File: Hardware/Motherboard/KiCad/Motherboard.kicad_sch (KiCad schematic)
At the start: 0 parts

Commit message: Added Motherboard schematic Rev. 1.0
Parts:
- added BZ1: Buzzer, Connector_PinHeader_2.54mm:PinHeader_1x02_P2.54mm_Vertical, symbol Device:Buzzer
- added C1: 10nF, Capacitor_SMD:C_1206_3216Metric_Pad1.33x1.80mm_HandSolder, symbol Device:C
- added C2: 100uF, Capacitor_SMD:CP_Elec_6.3x5.4, symbol Device:C_Polarized
- added D1: 1N4148WS, Diode_SMD:D_SOD-323_HandSoldering, symbol Device:D
- added H1, H2: M3, MountingHole:MountingHole_3.2mm_M3_Pad_Via, symbol Mechanical:MountingHole_Pad
- added J1: USB, Connector_PinHeader_2.54mm:PinHeader_1x04_P2.54mm_Vertical, symbol Connector_Generic:Conn_01x04
- added J2: FOLLOWER TUBE(S), Connector_PinHeader_2.54mm:PinHeader_1x03_P2.54mm_Vertical, symbol Connector_Generic:Conn_01x03
- added J3: MAIN TUBE(S), Connector_PinHeader_2.54mm:PinHeader_1x03_P2.54mm_Vertical, symbol Connector_Generic:Conn_01x03
- added Q1, Q2, Q3, Q4, Q5, Q6: MMBT3904, Package_TO_SOT_SMD:SOT-23, symbol Transistor_BJT:MMBT3904
- added Q7, Q8: MMBT3906, Package_TO_SOT_SMD:SOT-23, symbol Transistor_BJT:MMBT3906
- added R1: (Current Limit / Volume Adj.), Resistor_SMD:R_1206_3216Metric_Pad1.30x1.75mm_HandSolder, symbol Device:R
- added R10, R11, R12, R13, R14, R3, R4, R5, R6, R7, R8, R9: 10k, Resistor_SMD:R_1206_3216Metric_Pad1.30x1.75mm_HandSolder, symbol Device:R
- added R2: 1k, Resistor_SMD:R_1206_3216Metric_Pad1.30x1.75mm_HandSolder, symbol Device:R
- added U1: ~, Footprints:YD-ESP32-S3_(ESP32-S3-DevKitC-1_USB-C_Clone), symbol Symbols:YD-ESP32-S3_(ESP32-S3-DevKitC-1_USB-C_Clone)
- added U2: ~, Footprints:3.2in_SPI_TFT_Touch_Screen_&_SD_Card_Module, symbol Symbols:3.2in_SPI_TFT_Touch_Screen_&_SD_Card_Module
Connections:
- new net: Q8.1 (B), R8.1
- new net: Q3.3 (C), R7.2, R8.2
- new net: J2.2 (Pin_2), Q2.1 (B), R3.2
- new net: Q2.3 (C), R5.1, R6.1
- new net: Q5.3 (C), Q6.1 (B), R13.2
- new net: Q7.1 (B), R6.2
- new net: BZ1.1 (+), D1.1 (K), R1.2
- new net: BZ1.2 (-), D1.2 (A), Q1.3 (C)
- new net: Q4.1 (B), R12.1
- new net: Q4.3 (C), Q5.2 (E)
- new net: J3.2 (Pin_2), Q3.1 (B), R4.2
- new net: Q1.1 (B), R2.2
- new net: Q5.1 (B), R11.1
- new net: J1.3 (Pin_3), U1.25 (19)
- new net: J1.2 (Pin_2), U1.26 (20)
- new net +3V3: Q7.2 (E), Q8.2 (E), R13.1, R14.1, R5.2, R7.1, U1.1 (3V3), U1.2 (3V3)
- new net +5V: C1.1, C2.1, J1.1 (Pin_1), J2.1 (Pin_1), J3.1 (Pin_1), R1.1, U1.21 (5Vin), U2.1 (VCC)
- new net BUZZER: R2.1, U1.29 (48)
- new net COINCIDENCE_TRG: Q6.3 (C), R14.2, U1.37 (40)
- new net DISPLAY_CS: U1.11 (18), U2.3 (D_CS)
- new net DISPLAY_DC: U1.13 (3), U2.5 (D_DC)
- new net DISPLAY_LED: U1.15 (9), U2.8 (D_LED)
- new net DISPLAY_RST: U1.12 (8), U2.4 (D_RST)
- new net FOLLOWER_TRG: Q7.3 (C), R11.2, R9.2, U1.38 (41)
- new net GND: C1.2, C2.2, H1.1, H2.1, J1.4 (Pin_4), J2.3 (Pin_3), J3.3 (Pin_3), Q1.2 (E), Q2.2 (E), Q3.2 (E), Q4.2 (E), Q6.2 (E), R10.1, R3.1, R4.1, R9.1, U1.22 (GND), U1.23 (GND), U1.24 (GND), U1.44 (GND), U2.2 (GND)
- new net MAIN_TRG: Q8.3 (C), R10.2, R12.2, U1.39 (42)
- new net MISO: U1.19 (13), U2.13 (T_MISO), U2.17 (SD_MISO), U2.9 (D_MISO)
- new net MOSI: U1.17 (11), U2.12 (T_MOSI), U2.16 (SD_MOSI), U2.6 (D_MOSI)
- new net SCLK: U1.18 (12), U2.10 (T_SCLK), U2.18 (SD_SCLK), U2.7 (D_SCLK)
- new net SD_CD: U1.10 (17), U2.15 (SD_CS)
- new net TOUCH_CS: U1.16 (10), U2.11 (T_CS)
- new net TOUCH_IRQ: U1.20 (14), U2.14 (T_IRQ)
- no-connect marks 0 -> 21
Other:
- note added: "Buzzer Driver"
- note added: "Microcontroller"
- note added: "Mounting"
- note added: "Pulse Combiner & Coincidence Counter"
- note added: "Size: 3.2 inch Resolution: 240x320 px Display driver: ILI9341 Touch driver: XPT2046"
- note added: "Touchscreen & SD Card"
- note added: "YD-ESP32-S3 (ESP32-S3-DevKitC-1 USB-C Clone)"

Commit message: Motherboard PCB Rev. 1.0
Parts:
- J1: footprint Connector_PinHeader_2.54mm:PinHeader_1x04_P2.54mm_Vertical -> Footprints:USB_Pin_Header
- Q1, Q2, Q3, Q4, Q5, Q6, Q7, Q8: footprint Package_TO_SOT_SMD:SOT-23 -> Package_TO_SOT_SMD:SOT-23_Handsoldering
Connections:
- net BUZZER: now also U1.28 (47); no longer U1.29 (48)
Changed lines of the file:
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@@
 	(title_block
 		(title "Motherboard")
-		(date "2024-09-06")
+		(date "2024-09-07")
 		(rev "1.0")
 		(company "https://github.com/median-dispersion/GMT-Geiger-Counter")
@@
 	)
 	(no_connect
-		(at 236.22 77.47)
-	)
-	(no_connect
 		(at 236.22 62.23)
 	)
@@
 	)
 	(no_connect
+		(at 236.22 74.93)
+	)
+	(no_connect
 		(at 236.22 59.69)
 	)
@@
 	(wire
 		(pts
+			(xy 237.49 74.93) (xy 240.03 74.93)
+		)
+		(stroke
+			(width 0)
+			(type default)
+		)
+	)
+	(wire
+		(pts
 			(xy 240.03 90.17) (xy 256.54 90.17)
 		)
@@
 	(wire
 		(pts
+			(xy 236.22 77.47) (xy 237.49 77.47)
+		)
+		(stroke
+			(width 0)
+			(type default)
+		)
+	)
+	(wire
+		(pts
 			(xy 99.06 34.29) (xy 99.06 36.83)
 		)
@@
 	(wire
 		(pts
+			(xy 237.49 77.47) (xy 237.49 74.93)
+		)
+		(stroke
+			(width 0)
+			(type default)
+		)
+	)
+	(wire
+		(pts
 			(xy 214.63 146.05) (xy 214.63 140.97)
 		)
@@
 	(global_label "BUZZER"
 		(shape input)
-		(at 236.22 74.93 0)
+		(at 240.03 74.93 0)
 		(fields_autoplaced yes)
 		(effects
@@
 		)
 		(property "Intersheetrefs" "${INTERSHEET_REFS}"
-			(at 246.6437 74.93 0)
+			(at 250.4537 74.93 0)
 			(effects
 				(font
@@
 			)
 		)
-		(property "Footprint" "Package_TO_SOT_SMD:SOT-23"
+		(property "Footprint" "Package_TO_SOT_SMD:SOT-23_Handsoldering"
 			(at 77.47 53.975 0)
 			(effects
@@
 			)
 		)
-		(property "Footprint" "Package_TO_SOT_SMD:SOT-23"
+		(property "Footprint" "Package_TO_SOT_SMD:SOT-23_Handsoldering"
 			(at 92.71 43.815 0)
 			(effects
@@
 			)
 		)
-		(property "Footprint" "Package_TO_SOT_SMD:SOT-23"
+		(property "Footprint" "Package_TO_SOT_SMD:SOT-23_Handsoldering"
 			(at 116.84 56.515 0)
 			(effects
@@
 			)
 		)
-		(property "Footprint" "Package_TO_SOT_SMD:SOT-23"
+		(property "Footprint" "Package_TO_SOT_SMD:SOT-23_Handsoldering"
 			(at 134.62 92.075 0)
 			(effects
@@
 			)
 		)
-		(property "Footprint" "Package_TO_SOT_SMD:SOT-23"
+		(property "Footprint" "Package_TO_SOT_SMD:SOT-23_Handsoldering"
 			(at 57.15 154.305 0)
 			(effects
@@
 			)
 		)
-		(property "Footprint" "Package_TO_SOT_SMD:SOT-23"
+		(property "Footprint" "Package_TO_SOT_SMD:SOT-23_Handsoldering"
 			(at 134.62 81.915 0)
 			(effects
@@
 			)
 		)
-		(property "Footprint" "Package_TO_SOT_SMD:SOT-23"
+		(property "Footprint" "Package_TO_SOT_SMD:SOT-23_Handsoldering"
 			(at 101.6 66.675 0)
 			(effects
@@
 			)
 		)
-		(property "Footprint" "Package_TO_SOT_SMD:SOT-23"
+		(property "Footprint" "Package_TO_SOT_SMD:SOT-23_Handsoldering"
 			(at 149.86 74.295 0)
 			(effects
@@
 			)
 		)
-		(property "Footprint" "Connector_PinHeader_2.54mm:PinHeader_1x04_P2.54mm_Vertical"
+		(property "Footprint" "Footprints:USB_Pin_Header"
 			(at 246.38 82.55 0)
 			(effects

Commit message: Added BoM for motherboard
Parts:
- BZ1: DigiKey (none) -> https://www.digikey.com/en/products/detail/soberton-inc/WT-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; MPN (none) -> WT-1209T; Price (EUR) (none) -> 0,39€
- C1: DigiKey (none) -> https://www.digikey.com/en/products/detail/w%C3%BCrth-elekt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; MPN (none) -> 885012208112; Price (EUR) (none) -> 0,1€
- C2: DigiKey (none) -> https://www.digikey.com/en/products/detail/w%C3%BCrth-elekt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; MPN (none) -> 865080243007; Price (EUR) (none) -> 0,25€
- D1: DigiKey (none) -> https://www.digikey.com/en/products/detail/smc-diode-soluti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; MPN (none) -> 1N4148WS; Price (EUR) (none) -> 0,09€
- J1: DigiKey (none) -> https://www.digikey.com/en/products/detail/adam-tech/PH1RB-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; MPN (none) -> PH1RB-04-UA; Price (EUR) (none) -> 0,14€
- J2, J3: DigiKey (none) -> https://www.digikey.com/en/products/detail/adam-tech/PH1RB-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; MPN (none) -> PH1RB-03-UA; Price (EUR) (none) -> 0,11€
- Q1, Q2, Q3, Q4, Q5, Q6: DigiKey (none) -> https://www.digikey.com/en/products/detail/good-ark-semicon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; MPN (none) -> MMBT3904; Price (EUR) (none) -> 0,09€
- Q7, Q8: DigiKey (none) -> https://www.digikey.com/en/products/detail/good-ark-semicon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; MPN (none) -> MMBT3906; Price (EUR) (none) -> 0,09€
- R1: DigiKey (none) -> https://www.digikey.com/en/products/detail/yageo/RC1206JR-0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; MPN (none) -> RC1206JR-070RL; Price (EUR) (none) -> 0,09€
- R10, R11, R12, R13, R14, R3, R4, R5, R6, R7, R8, R9: DigiKey (none) -> https://www.digikey.com/en/products/detail/yageo/RC1206FR-1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; MPN (none) -> RC1206FR-1310KL; Price (EUR) (none) -> 0,09€
- R2: DigiKey (none) -> https://www.digikey.com/en/products/detail/yageo/RC1206FR-0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; MPN (none) -> RC1206FR-071KL; Price (EUR) (none) -> 0,09€
- U1: value ~ -> YD-ESP32-S3 N16R8 (ESP32-S3-DevKitC-1 USB-C Clone); MPN (none) -> YD-ESP32-S3 N16R8; Price (EUR) (none) -> 8€
- U2: value ~ -> MSP3218; MPN (none) -> MSP3218; Price (EUR) (none) -> 12€
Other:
- note removed: "YD-ESP32-S3 (ESP32-S3-DevKitC-1 USB-C Clone)"

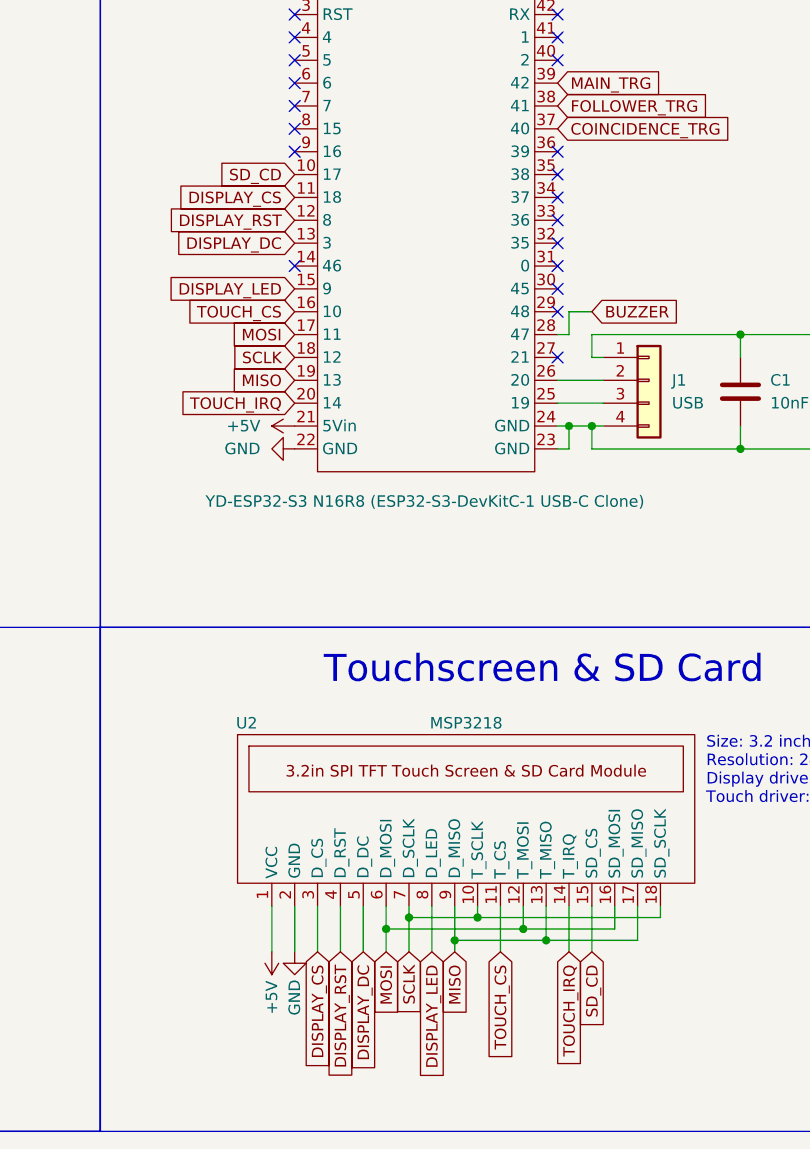
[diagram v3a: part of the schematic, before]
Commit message: Changed component value, fixed typos & fixed small mistakes
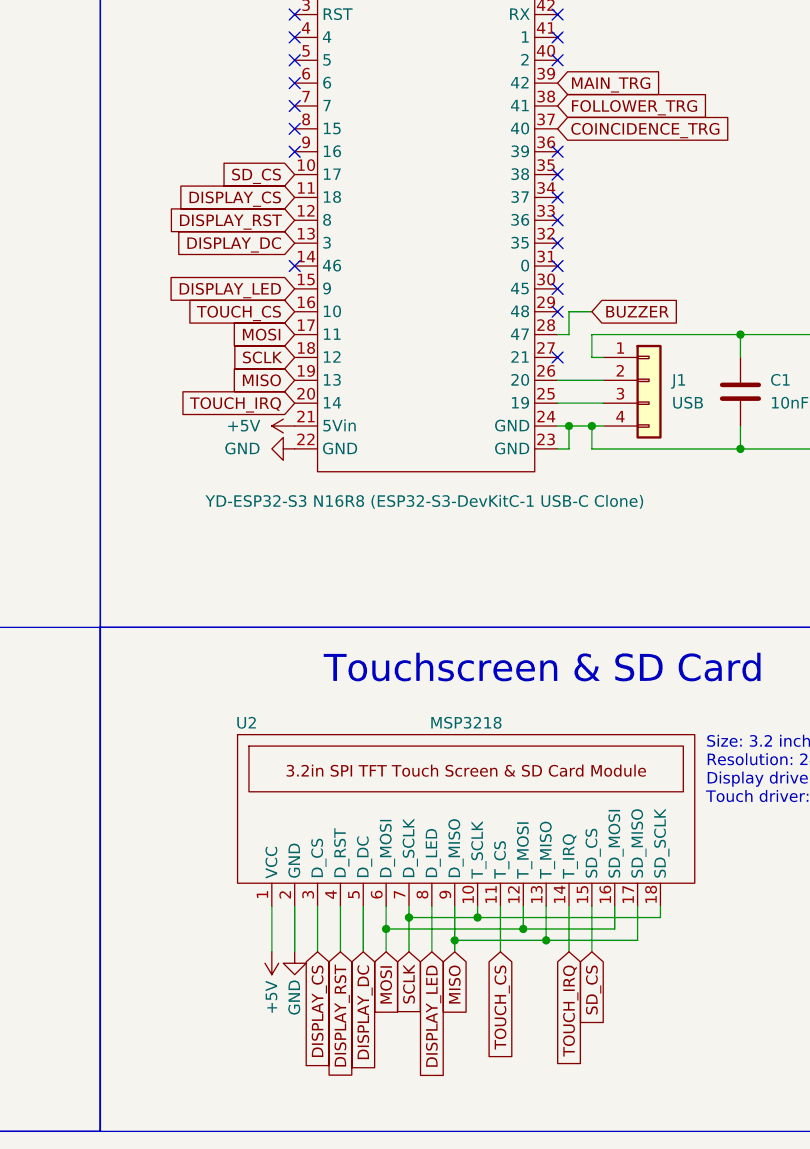
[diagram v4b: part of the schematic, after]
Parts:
- C2: DigiKey https://www.digikey.com/en/products/detail/w%C3%BCrth-elekt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 -> https://www.digikey.com/en/products/detail/würth-elektronik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; MPN 865080243007 -> 875105344010; Price (EUR) 0,25€ -> 0,62€
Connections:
- net SD_CD renamed SD_CS
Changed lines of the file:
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@@
 	(title_block
 		(title "Motherboard")
-		(date "2024-09-10")
+		(date "2024-11-14")
 		(rev "1.0")
 		(company "https://github.com/median-dispersion/GMT-Geiger-Counter")
@@
 		)
 	)
-	(global_label "SD_CD"
+	(global_label "SD_CS"
 		(shape input)
 		(at 207.01 59.69 180)
@@
 		)
 		(property "Intersheetrefs" "${INTERSHEET_REFS}"
-			(at 198.0377 59.69 0)
+			(at 198.0982 59.69 0)
 			(effects
 				(font
@@
 		)
 	)
-	(global_label "SD_CD"
+	(global_label "SD_CS"
 		(shape input)
 		(at 240.03 146.05 270)
@@
 		)
 		(property "Intersheetrefs" "${INTERSHEET_REFS}"
-			(at 240.03 155.0223 90)
+			(at 240.03 154.9618 90)
 			(effects
 				(font
@@
 			)
 		)
-		(property "Datasheet" "https://www.we-online.com/components/products/datasheet/865080243007.pdf"
+		(property "Datasheet" "https://www.we-online.com/components/products/datasheet/875105344010.pdf"
 			(at 267.97 83.82 0)
 			(effects
@@
 			)
 		)
-		(property "DigiKey" "https://www.digikey.com/en/products/detail/w%C3%BCrth-elektronik/865080243007/5728085 "
+		(property "DigiKey" "https://www.digikey.com/en/products/detail/würth-elektronik/875105344010/5147589"
 			(at 267.97 83.82 0)
 			(effects
@@
 			)
 		)
-		(property "MPN" "865080243007 "
+		(property "MPN" "875105344010"
 			(at 267.97 83.82 0)
 			(effects
@@
 			)
 		)
-		(property "Price (EUR)" "0,25€ "
+		(property "Price (EUR)" "0,62€"
 			(at 267.97 83.82 0)
 			(effects

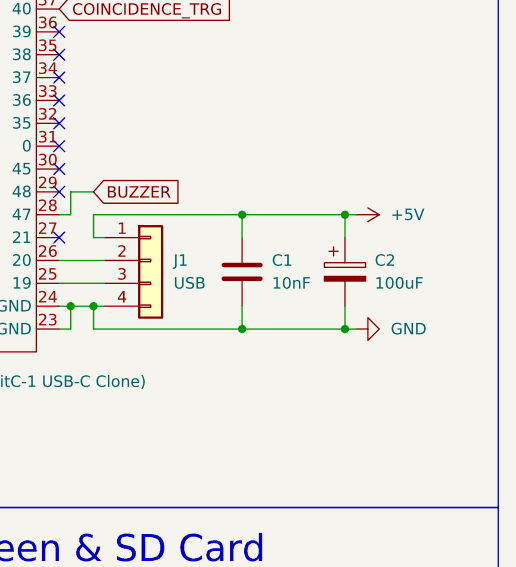
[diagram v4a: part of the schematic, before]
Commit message: Updated the decoupling capacitor to make it more USB 'compliant'
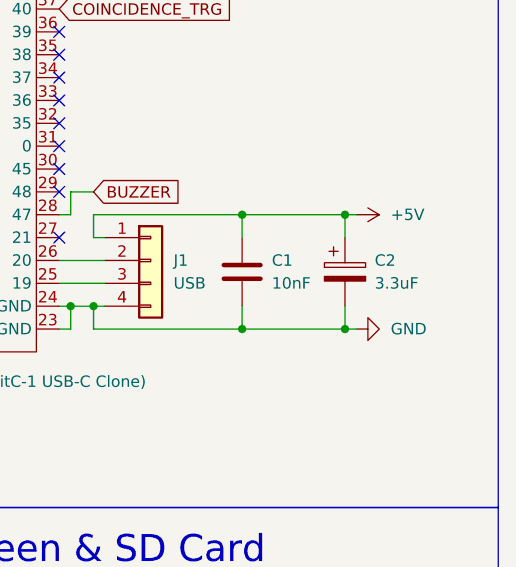
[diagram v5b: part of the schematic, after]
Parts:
- C2: value 100uF -> 3.3uF; DigiKey https://www.digikey.com/en/products/detail/würth-elektronik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 -> https://www.digikey.com/en/products/detail/panasonic-electr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; MPN 875105344010 -> 16SVP3R3M; Price (EUR) 0,62€ -> 0,75€
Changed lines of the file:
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@@
 			)
 		)
-		(property "Value" "100uF"
+		(property "Value" "3.3uF"
 			(at 271.272 85.09 0)
 			(effects
@@
 			)
 		)
-		(property "Datasheet" "https://www.we-online.com/components/products/datasheet/875105344010.pdf"
+		(property "Datasheet" "https://industrial.panasonic.com/ww/products/pt/os-con/models/16SVP3R3M"
 			(at 267.97 83.82 0)
 			(effects
@@
 			)
 		)
-		(property "DigiKey" "https://www.digikey.com/en/products/detail/würth-elektronik/875105344010/5147589"
+		(property "DigiKey" "https://www.digikey.com/en/products/detail/panasonic-electronic-components/16svp3r3m/4204797"
 			(at 267.97 83.82 0)
 			(effects
@@
 			)
 		)
-		(property "MPN" "875105344010"
+		(property "MPN" "16SVP3R3M"
 			(at 267.97 83.82 0)
 			(effects
@@
 			)
 		)
-		(property "Price (EUR)" "0,62€"
+		(property "Price (EUR)" "0,75€"
 			(at 267.97 83.82 0)
 			(effects
